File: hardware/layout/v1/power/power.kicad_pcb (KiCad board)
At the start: 4 copper layers, 28.5 x 30 mm, 33 parts, among them J1 Main board, U1 SCT2430STER, U2 SCT2430STER

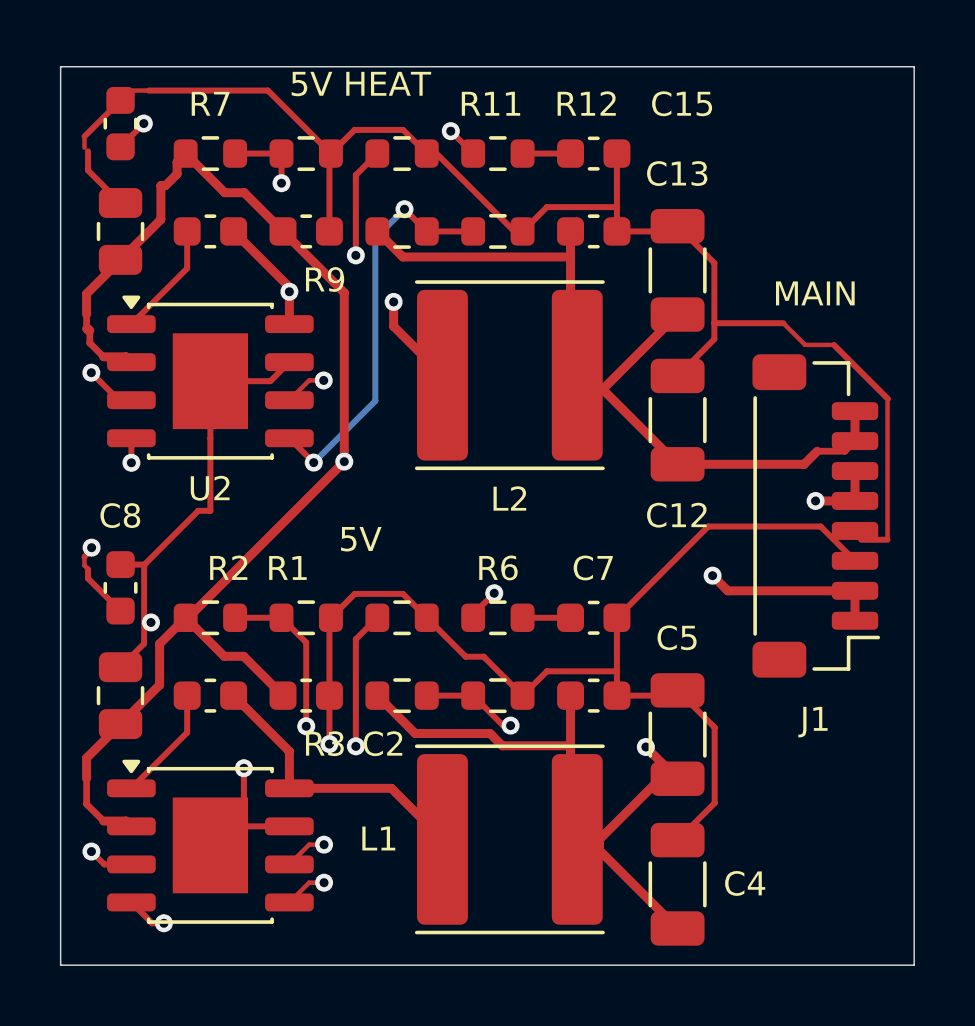
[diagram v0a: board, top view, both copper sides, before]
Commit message: Update documentation for 60V power system, STM32 crown board, 12V heaters, and expanded enclosure design
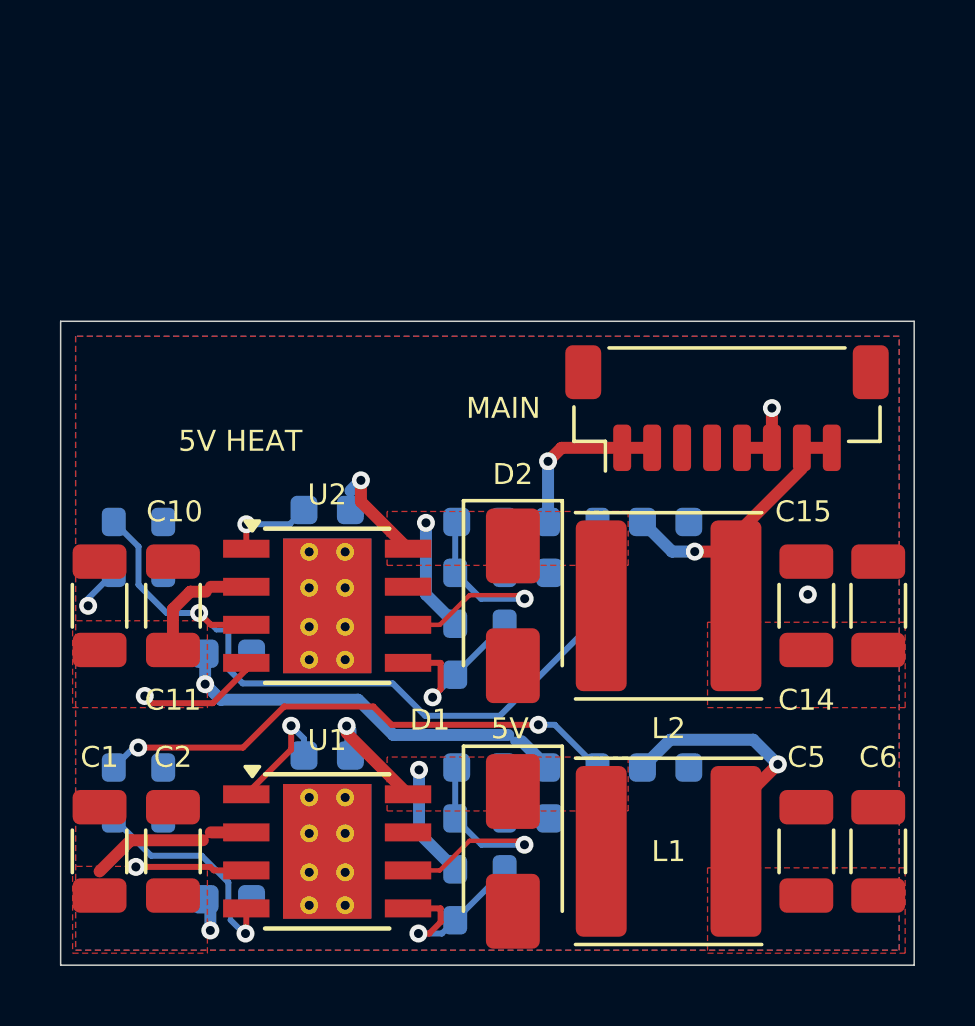
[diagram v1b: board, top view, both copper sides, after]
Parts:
- added C17: 18n 50V, Capacitor_SMD:C_0603_1608Metric, B.Cu at (17.1, -13.1)
- added C18: 68p C0G 50V, Capacitor_SMD:C_0603_1608Metric, B.Cu at (14.0, -14.8)
- added D1: B360A, Diode_SMD:D_SMA, F.Cu at (15.1, -3.80)
- added D2: B360A, Diode_SMD:D_SMA, F.Cu at (15.1, -12.0)
- C1: value 10u 50V -> 2u2 100V; footprint Capacitor_SMD:C_0805_2012Metric -> Capacitor_SMD:C_1206_3216Metric
- C10, C11, C2: value 100n 50V -> 2u2 100V; footprint Capacitor_SMD:C_0603_1608Metric -> Capacitor_SMD:C_1206_3216Metric
- C12: value 47u 10V -> 100n 100V; footprint Capacitor_SMD:C_1206_3216Metric -> Capacitor_SMD:C_0603_1608Metric; moved to B.Cu
- C13, C4: value 47u 10V -> 100n 50V; footprint Capacitor_SMD:C_1206_3216Metric -> Capacitor_SMD:C_0603_1608Metric; moved to B.Cu
- C14: value 100n 50V -> 22u 25V; footprint Capacitor_SMD:C_0603_1608Metric -> Capacitor_SMD:C_1206_3216Metric
- C15: value 3n3 50V -> 22u 25V; footprint Capacitor_SMD:C_0603_1608Metric -> Capacitor_SMD:C_1206_3216Metric
- C16: value 22p C0G 50V -> 100n 50V; moved to B.Cu
- C3: value 100n 50V -> 100n 100V; moved to B.Cu
- C6: value 100n 50V -> 47u 10V; footprint Capacitor_SMD:C_0603_1608Metric -> Capacitor_SMD:C_1206_3216Metric
- C7: value 3n3 50V -> 100n 50V; moved to B.Cu
- C8: value 22p C0G 50V -> 33n 50V; moved to B.Cu
- C9: value 10u 50V -> 68p C0G 50V; footprint Capacitor_SMD:C_0805_2012Metric -> Capacitor_SMD:C_0603_1608Metric; moved to B.Cu
- L2: value 8.2uH -> 22uH
- R1, R7: value 51k -> 511k; moved to B.Cu
- R10: value 10k2 -> 10k; moved to B.Cu
- R11, R5: value 200k -> 130k; moved to B.Cu
- R12, R6: value 33k2 -> 6k49; moved to B.Cu
- R2, R8: value 10k -> 82k5; moved to B.Cu
- R3, R4: moved to B.Cu
- R9: value 53k6 -> 140k; moved to B.Cu
- U1, U2: value SCT2430STER -> TPS54360DDAR; footprint Package_SO:SOIC-8-1EP_3.9x4.9mm_P1.27mm_EP2.514x3.2mm -> Package_SO:TI_SO-PowerPAD-8_ThermalVias
- moved C16 22.5 mm to (20.2, -14.8), turned to 0 degrees
- moved C9 21.6 mm to (14.0, -6.60), turned to 0 degrees
- moved C15 17.8 mm to (27.3, -12.0), turned to 90 degrees
- moved R7 17.3 mm to (17.1, -14.8)
- moved C8 16.9 mm to (17.1, -4.90), turned to 0 degrees
- moved C12 16.9 mm to (5.60, -10.4), turned to 0 degrees
- moved R11 16.5 mm to (2.60, -13.1)
- moved R10 14.8 mm to (14.0, -9.70)
- moved C14 14.4 mm to (24.9, -12.0), turned to 90 degrees
- moved C10 14.3 mm to (1.30, -12.0), turned to 90 degrees
- moved C13 14.2 mm to (8.90, -15.2), turned to 0 degrees
- moved R12 14.0 mm to (14.0, -13.1)
- moved R8 13.5 mm to (2.60, -14.8)
- moved R9 13.4 mm to (14.0, -11.4)
- moved R1 13.1 mm to (17.1, -6.60)
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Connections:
- C11 pad 1: HEAT_BST -> VIN_PROT
- C11 pad 2: HEAT_SW -> GND
- C12 pad 1: +5V_HEAT -> VIN_PROT
- C13 pad 1: +5V_HEAT -> HEAT_BST
- C13 pad 2: GND -> HEAT_SW
- C14 pad 1: +5V_HEAT -> +12V_HEAT
- C15 pad 1: HEAT_CC -> +12V_HEAT
- C16 pad 1: HEAT_COMP -> +12V_HEAT
- C3 pad 1: LOGIC_BST -> VIN_PROT
- C3 pad 2: LOGIC_SW -> GND
- C4 pad 1: +5V -> LOGIC_BST
- C4 pad 2: GND -> LOGIC_SW
- C7 pad 1: LOGIC_CC -> +5V
- C8 pad 1: LOGIC_COMP -> LOGIC_CC
- C9 pad 1: VIN_PROT -> LOGIC_COMP
- J1 pad 7: +5V_HEAT -> +12V_HEAT
- J1 pad 8: +5V_HEAT -> +12V_HEAT
- L2 pad 2: +5V_HEAT -> +12V_HEAT
- R9 pad 1: +5V_HEAT -> +12V_HEAT
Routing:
- net GND: track 102.1 -> 0.00 mm, vias 3 -> 1
- net +5V_HEAT: track 27.1 -> 0.00 mm
- net +12V_HEAT: track 0.00 -> 23.3 mm, vias 0 -> 2
- net LOGIC_COMP: track 30.1 -> 8.75 mm, vias 3 -> 1
- net HEAT_COMP: track 25.1 -> 8.75 mm, vias 3 -> 1
- net HEAT_EN: track 13.7 -> 27.3 mm, vias 2 -> 1
- net VIN_PROT: track 63.4 -> 51.9 mm, vias 2 -> 3
- net LOGIC_EN: track 15.9 -> 25.6 mm, vias 2 -> 3
- net HEAT_RT: track 17.6 -> 9.43 mm
- net HEAT_FB: track 13.5 -> 5.80 mm, vias 2 -> 1
- net LOGIC_RT: track 14.8 -> 7.53 mm, vias 2 -> 1
- net HEAT_SW: track 10.6 -> 3.43 mm, vias 2 -> 1
- net LOGIC_FB: track 13.0 -> 6.24 mm, vias 2 -> 1
- net LOGIC_SW: track 9.69 -> 3.76 mm, vias 0 -> 1
- net +5V: track 34.7 -> 37.0 mm, vias 2 -> 3
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- added copper zone on F.Cu, net +12V_HEAT
- added copper zone on F.Cu, net +5V
- added copper zone on B.Cu, net GND
- added copper zone on F.Cu, net GND
- added copper zone on F.Cu, net HEAT_SW
- added copper zone on F.Cu, net LOGIC_SW
- added copper zone on F.Cu, net VIN_PROT
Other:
- board size 28.5 x 30 mm -> 28.5 x 21.5 mm

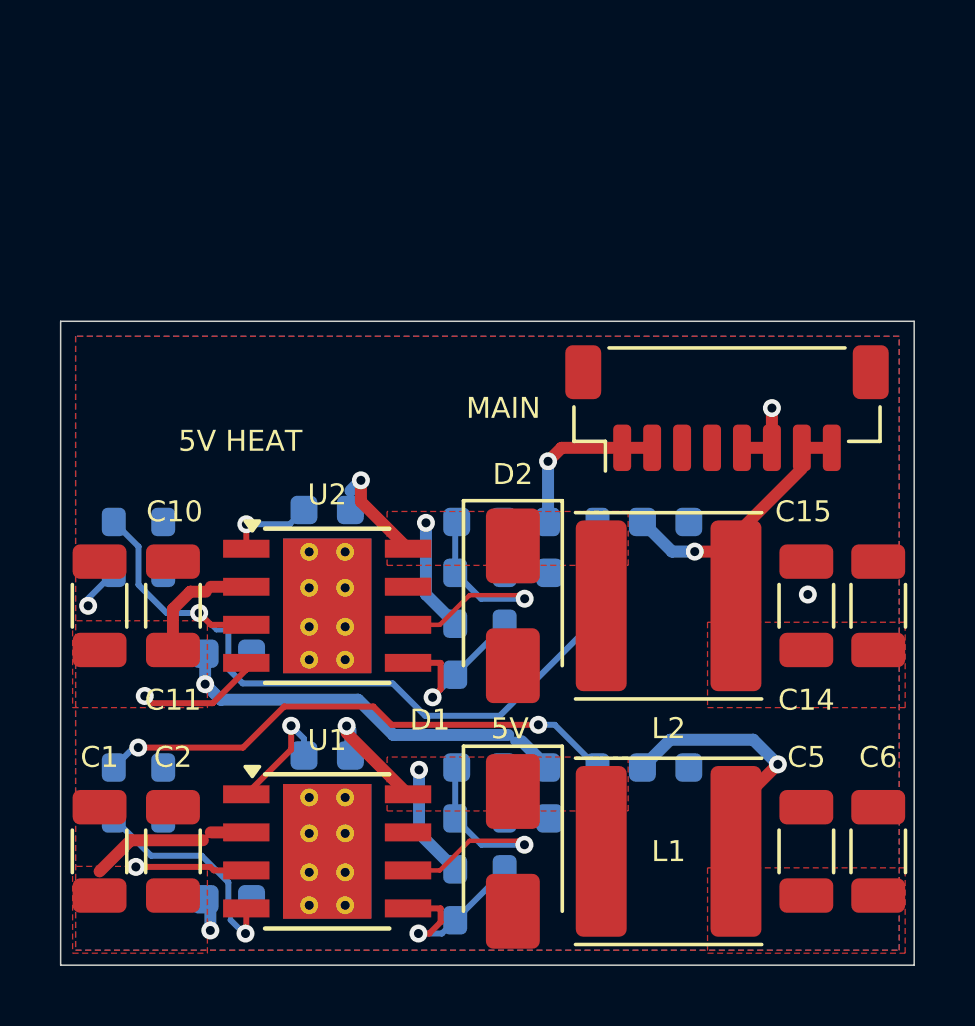
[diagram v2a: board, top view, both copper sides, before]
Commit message: Update documentation for column-packed breakaway panel, probe LDO rail, mast clamp dimensions, transducer adapter redesign, crown SWD/auto-flash workflow, and enclosure print plate organization
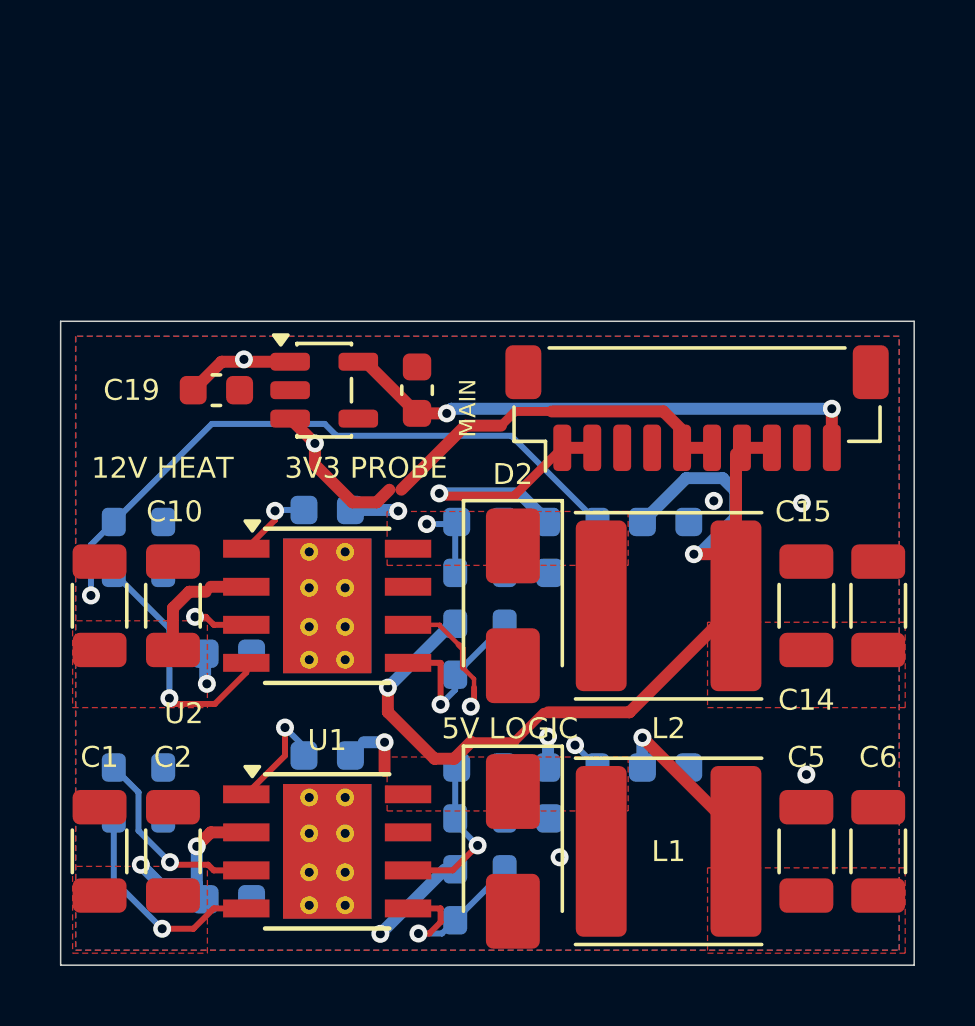
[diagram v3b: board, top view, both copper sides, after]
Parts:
- added C19: 1u 50V, Capacitor_SMD:C_0603_1608Metric, F.Cu at (5.20, -19.2)
- added C20: 10u 10V, Capacitor_SMD:C_0603_1608Metric, F.Cu at (11.9, -19.2)
- added U3: AP2112K-3.3, Package_TO_SOT_SMD:SOT-23-5, F.Cu at (8.80, -19.2)
- J1: footprint Connector_JST:JST_SH_BM08B-SRSS-TB_1x08-1MP_P1.00mm_Vertical -> Connector_JST:JST_SH_BM10B-SRSS-TB_1x10-1MP_P1.00mm_Vertical
- moved J1 1.00 mm to (21.2, -18.6)
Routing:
- net +5V: track 37.0 -> 59.6 mm, vias 3 -> 4
- net +3V3_PROBE: track 0.00 -> 17.9 mm, vias 0 -> 2
- net +12V_HEAT: track 23.3 -> 30.3 mm
- net HEAT_COMP: track 8.75 -> 13.7 mm, vias 1 -> 2
- net VIN_PROT: track 51.9 -> 47.0 mm, vias 3 -> 5
- net LOGIC_COMP: track 8.75 -> 5.60 mm
- net LOGIC_EN: track 25.6 -> 22.9 mm, vias 3 -> 2
- net LOGIC_SW: track 3.76 -> 1.65 mm
- net HEAT_SW: track 3.43 -> 1.56 mm
- net HEAT_RT: track 9.43 -> 8.36 mm, vias 2 -> 1
- net HEAT_EN: track 27.3 -> 27.2 mm, vias 1 -> 2
- net GND: vias 1 -> 4
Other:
- board text added: "12V HEAT"
- board text added: "3V3 PROBE"
- board text added: "5V LOGIC"
- board text removed: "5V"
- board text removed: "5V HEAT"

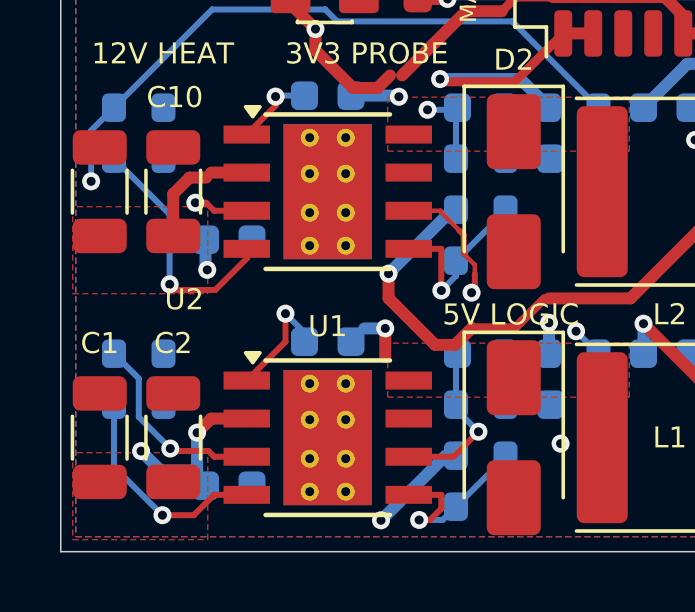
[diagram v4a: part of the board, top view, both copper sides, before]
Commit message: Update AGENTS.md, CALIBRATION.md, and README.md for PTFE dome diffuser, probe heater setpoint change to −7.6 °C, crown preamp bias mode, RS-485 fail-safe bias note, and enclosure seal test
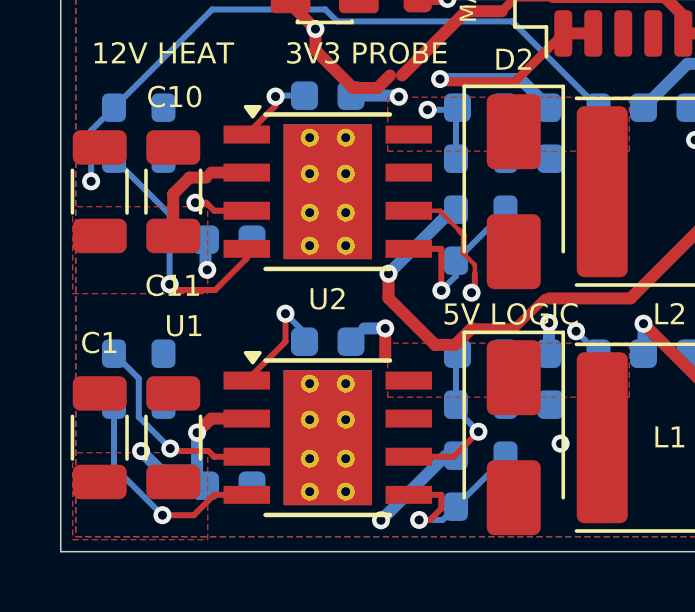
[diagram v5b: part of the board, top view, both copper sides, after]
